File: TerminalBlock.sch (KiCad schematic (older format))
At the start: 0 parts

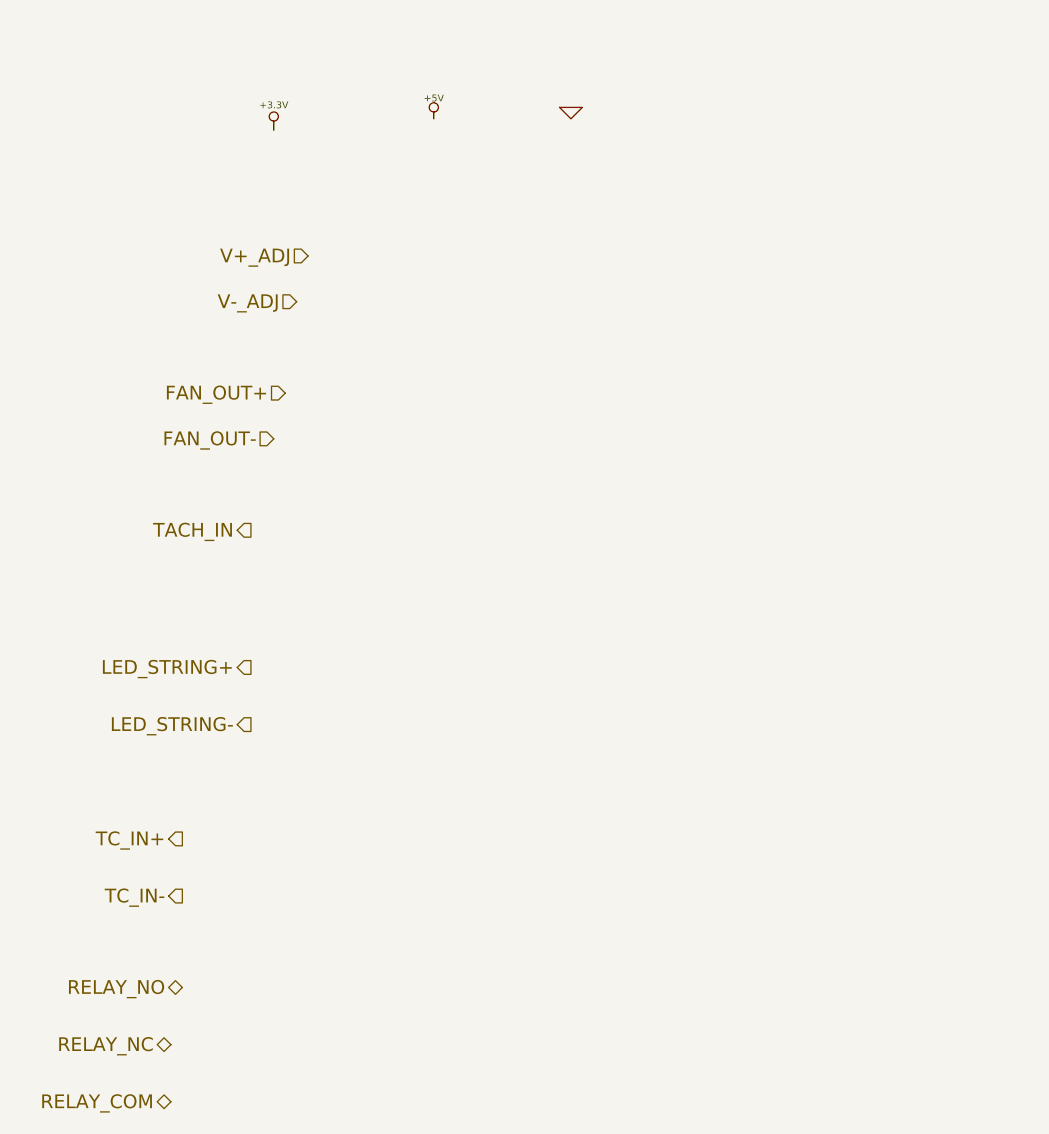
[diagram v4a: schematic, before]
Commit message: Placement of connectors
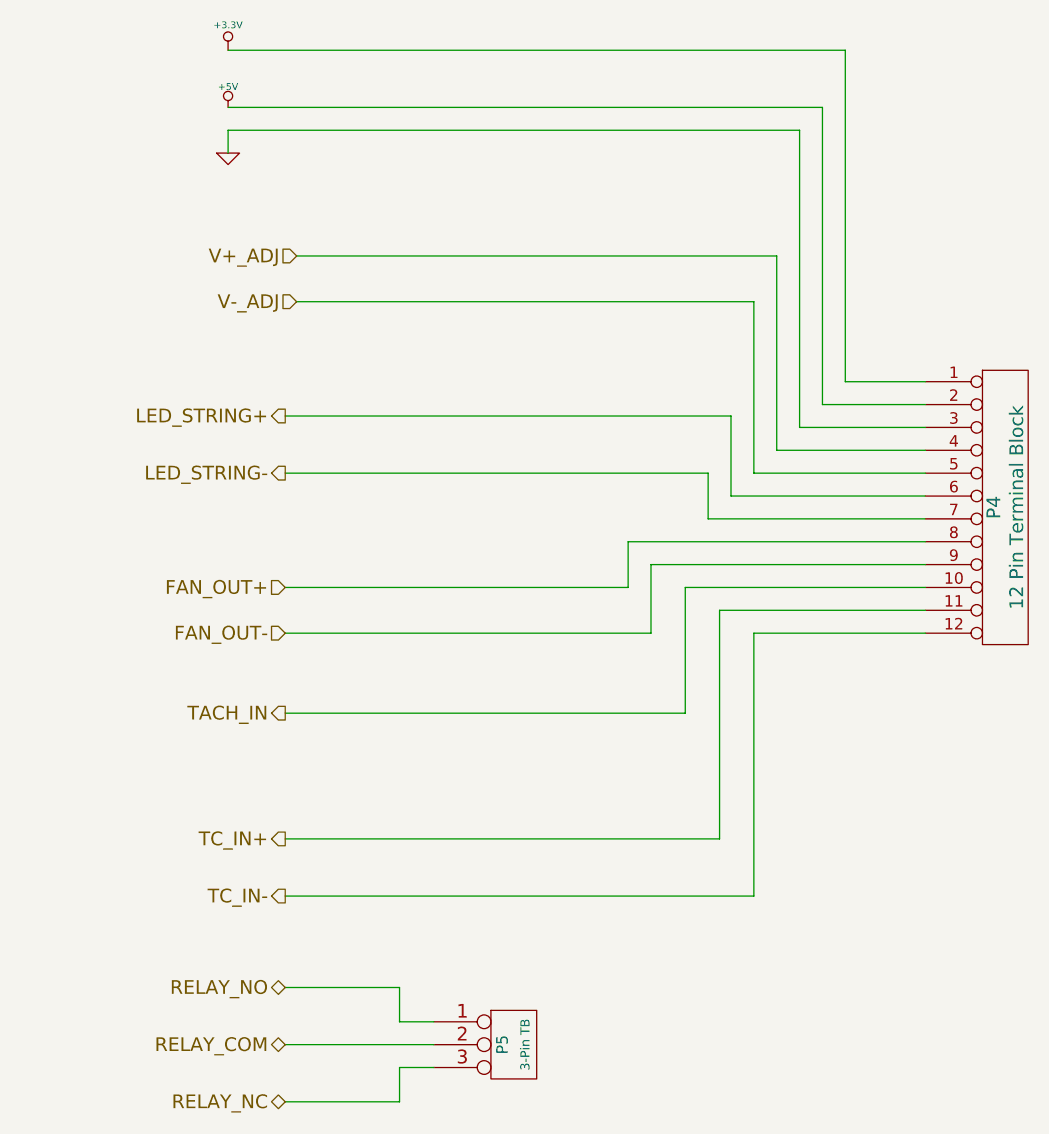
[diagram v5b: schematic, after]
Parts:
- added P4: 12 Pin Terminal Block, symbol CONN_12
- added P5: 3-Pin TB, symbol CONN_3
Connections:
- net +3.3V: now also P4.1 (P1)
- net +5V: now also P4.2 (P2)
- net FAN_OUT+: now also P4.8 (P8)
- net FAN_OUT-: now also P4.9 (P9)
- net GND: now also P4.3 (P3)
- net LED_STRING+: now also P4.6 (P6)
- net LED_STRING-: now also P4.7 (P7)
- net RELAY_COM: now also P5.2 (PM)
- net RELAY_NC: now also P5.3 (P3)
- net RELAY_NO: now also P5.1 (P1)
- net TACH_IN: now also P4.10 (P10)
- net TC_IN+: now also P4.11 (P11)
- net TC_IN-: now also P4.12 (P12)
- net V+_ADJ: now also P4.4 (P4)
- net V-_ADJ: now also P4.5 (P5)
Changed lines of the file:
@@
 $Descr A4 11693 8268
 encoding utf-8
-Sheet 8 9
+Sheet 7 9
 Title ""
 Date "4 feb 2014"
@@
 Comment4 ""
 $EndDescr
-Text HLabel 2300 1800 0    60   Input ~ 0
+Text HLabel 2250 1800 0    60   Input ~ 0
 V+_ADJ
 Text HLabel 2250 2000 0    60   Input ~ 0
 V-_ADJ
-Text HLabel 2200 2400 0    60   Input ~ 0
+Text HLabel 2200 3250 0    60   Input ~ 0
 FAN_OUT+
-Text HLabel 2150 2600 0    60   Input ~ 0
+Text HLabel 2200 3450 0    60   Input ~ 0
 FAN_OUT-
-Text HLabel 2050 3000 0    60   Output ~ 0
+Text HLabel 2200 3800 0    60   Output ~ 0
 TACH_IN
-Text HLabel 2050 3600 0    60   Output ~ 0
+Text HLabel 2200 2500 0    60   Output ~ 0
 LED_STRING+
-Text HLabel 2050 3850 0    60   Output ~ 0
+Text HLabel 2200 2750 0    60   Output ~ 0
 LED_STRING-
-Text HLabel 1750 4350 0    60   Output ~ 0
+Text HLabel 2200 4350 0    60   Output ~ 0
 TC_IN+
-Text HLabel 1750 4600 0    60   Output ~ 0
+Text HLabel 2200 4600 0    60   Output ~ 0
 TC_IN-
-Text HLabel 1750 5000 0    60   BiDi ~ 0
+Text HLabel 2200 5000 0    60   BiDi ~ 0
 RELAY_NO
-Text HLabel 1700 5250 0    60   BiDi ~ 0
+Text HLabel 2200 5500 0    60   BiDi ~ 0
 RELAY_NC
-Text HLabel 1700 5500 0    60   BiDi ~ 0
+Text HLabel 2200 5250 0    60   BiDi ~ 0
 RELAY_COM
 $Comp
-L +3.3V #PWR041
+L +3.3V #PWR41
 U 1 1 52F1764B
-P 2150 1250
-F 0 "#PWR041" H 2150 1210 30  0001 C CNN
-F 1 "+3.3V" H 2150 1360 30  0000 C CNN
-F 2 "" H 2150 1250 60  0000 C CNN
-F 3 "" H 2150 1250 60  0000 C CNN
-	1    2150 1250
+P 1950 900
+F 0 "#PWR41" H 1950 860 30  0001 C CNN
+F 1 "+3.3V" H 1950 1010 30  0000 C CNN
+F 2 "" H 1950 900 60  0000 C CNN
+F 3 "" H 1950 900 60  0000 C CNN
+	1    1950 900
 	1    0    0    -1
 $EndComp
 $Comp
-L +5V #PWR042
+L +5V #PWR42
 U 1 1 52F1765A
-P 2850 1200
-F 0 "#PWR042" H 2850 1290 20  0001 C CNN
-F 1 "+5V" H 2850 1290 30  0000 C CNN
-F 2 "" H 2850 1200 60  0000 C CNN
-F 3 "" H 2850 1200 60  0000 C CNN
-	1    2850 1200
+P 1950 1150
+F 0 "#PWR42" H 1950 1240 20  0001 C CNN
+F 1 "+5V" H 1950 1240 30  0000 C CNN
+F 2 "" H 1950 1150 60  0000 C CNN
+F 3 "" H 1950 1150 60  0000 C CNN
+	1    1950 1150
 	1    0    0    -1
 $EndComp
 $Comp
-L GND #PWR043
+L GND #PWR43
 U 1 1 52F17669
-P 3450 1150
-F 0 "#PWR043" H 3450 1150 30  0001 C CNN
-F 1 "GND" H 3450 1080 30  0001 C CNN
-F 2 "" H 3450 1150 60  0000 C CNN
-F 3 "" H 3450 1150 60  0000 C CNN
-	1    3450 1150
+P 1950 1350
+F 0 "#PWR43" H 1950 1350 30  0001 C CNN
+F 1 "GND" H 1950 1280 30  0001 C CNN
+F 2 "" H 1950 1350 60  0000 C CNN
+F 3 "" H 1950 1350 60  0000 C CNN
+	1    1950 1350
 	1    0    0    -1
 $EndComp
+$Comp
+L CONN_12 P4
+U 1 1 5303AD7E
+P 5350 2900
+F 0 "P4" V 5300 2900 60  0000 C CNN
+F 1 "12 Pin Terminal Block" V 5400 2900 60  0000 C CNN
+F 2 "" H 5350 2900 60  0000 C CNN
+F 3 "" H 5350 2900 60  0000 C CNN
+F 4 "On Shore" H 5350 2900 60  0001 C CNN "MFG Name"
+F 5 "OSTTE120104" H 5350 2900 60  0001 C CNN "MFG Part Number"
+	1    5350 2900
+	1    0    0    -1
+$EndComp
+Wire Wire Line
+	5000 2350 4650 2350
+Wire Wire Line
+	4650 2350 4650 900
+Wire Wire Line
+	4650 900  1950 900
+Wire Wire Line
+	1950 1150 4550 1150
+Wire Wire Line
+	4550 1150 4550 2450
+Wire Wire Line
+	4550 2450 5000 2450
+Wire Wire Line
+	5000 2550 4450 2550
+Wire Wire Line
+	4450 2550 4450 1250
+Wire Wire Line
+	4450 1250 1950 1250
+Wire Wire Line
+	1950 1250 1950 1350
+Wire Wire Line
+	5000 2650 4350 2650
+Wire Wire Line
+	4350 2650 4350 1800
+Wire Wire Line
+	4350 1800 2250 1800
+Wire Wire Line
+	2250 2000 4250 2000
+Wire Wire Line
+	4250 2000 4250 2750
+Wire Wire Line
+	4250 2750 5000 2750
+Wire Wire Line
+	2200 2500 4150 2500
+Wire Wire Line
+	4150 2500 4150 2850
+Wire Wire Line
+	4150 2850 5000 2850
+Wire Wire Line
+	2200 2750 4050 2750
+Wire Wire Line
+	4050 2750 4050 2950
+Wire Wire Line
+	4050 2950 5000 2950
+Wire Wire Line
+	2200 3250 3700 3250
+Wire Wire Line
+	3700 3250 3700 3050
+Wire Wire Line
+	3700 3050 5000 3050
+Wire Wire Line
+	2200 3450 3800 3450
+Wire Wire Line
+	3800 3450 3800 3150
+Wire Wire Line
+	3800 3150 5000 3150
+Wire Wire Line
+	2200 3800 3950 3800
+Wire Wire Line
+	3950 3800 3950 3250
+Wire Wire Line
+	3950 3250 5000 3250
+Wire Wire Line
+	2200 4350 4100 4350
+Wire Wire Line
+	4100 4350 4100 3350
+Wire Wire Line
+	4100 3350 5000 3350
+Wire Wire Line
+	5000 3450 4250 3450
+Wire Wire Line
+	4250 3450 4250 4600
+Wire Wire Line
+	4250 4600 2200 4600
+$Comp
+L CONN_3 P5
+U 1 1 5303AF1A
+P 3200 5250
+F 0 "P5" V 3150 5250 50  0000 C CNN
+F 1 "3-Pin TB" V 3250 5250 40  0000 C CNN
+F 2 "" H 3200 5250 60  0000 C CNN
+F 3 "" H 3200 5250 60  0000 C CNN
+F 4 "Phoenix Contact" H 3200 5250 60  0001 C CNN "MFG Name"
+F 5 "1935174" H 3200 5250 60  0001 C CNN "MFG Part Number"
+	1    3200 5250
+	1    0    0    -1
+$EndComp
+Wire Wire Line
+	2200 5000 2700 5000
+Wire Wire Line
+	2700 5000 2700 5150
+Wire Wire Line
+	2700 5150 2850 5150
+Wire Wire Line
+	2850 5250 2200 5250
+Wire Wire Line
+	2850 5350 2700 5350
+Wire Wire Line
+	2700 5350 2700 5500
+Wire Wire Line
+	2700 5500 2200 5500
 $EndSCHEMATC
